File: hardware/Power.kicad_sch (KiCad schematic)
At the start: 51 parts, among them U10 LDK320ADU120R, U4 TPS563300DRLR, U5 TPS563219ADDFR, U6 LM2940SX-12_NOPB, U7 LM1117IMP-5.0, U8 TLV743P, U9 AP2127N3-1.5

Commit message: Added Voltage reference, fixed silkscreen and BOM
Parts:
- U5: footprint SOT65P280X110-8N -> TPS563219ADDFR:SOT65P280X110-8N
- U6: footprint KTT0003B -> DDPAK:KTT0003B
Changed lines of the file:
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@@
 			)
 		)
-		(property "Datasheet" "~"
+		(property "Datasheet" "---"
 			(at 77.47 166.37 0)
 			(effects
@@
 			)
 		)
-		(property "Datasheet" "~"
+		(property "Datasheet" "---"
 			(at 208.28 119.38 0)
 			(effects
@@
 			)
 		)
-		(property "Footprint" "KTT0003B"
+		(property "Footprint" "DDPAK:KTT0003B"
 			(at 66.04 214.3 0)
 			(effects
@@
 			)
 		)
-		(property "Datasheet" "~"
+		(property "Datasheet" "---"
 			(at 163.83 35.56 0)
 			(effects
@@
 			)
 		)
-		(property "Datasheet" "~"
+		(property "Datasheet" "---"
 			(at 139.7 119.38 0)
 			(effects
@@
 			)
 		)
-		(property "Datasheet" "~"
+		(property "Datasheet" "---"
 			(at 144.78 166.37 0)
 			(effects
@@
 			)
 		)
-		(property "Datasheet" "~"
+		(property "Datasheet" "---"
 			(at 152.4 73.66 0)
 			(effects
@@
 			)
 		)
-		(property "Datasheet" "https://www.littelfuse.com/assetdocs/littelfuse_fuse_466_datasheet?assetguid=dbe9bcd7-6072-4adf-bf5b-d33e52a6b90f"
+		(property "Datasheet" "https://www.mouser.pl/datasheet/3/40/1/sf0603f.pdf"
 			(at 95.25 119.38 0)
 			(effects
@@
 			)
 		)
-		(property "Footprint" "SOT65P280X110-8N"
+		(property "Footprint" "TPS563219ADDFR:SOT65P280X110-8N"
 			(at 95.25 168.58 0)
 			(effects
@@
 			)
 		)
-		(property "Datasheet" "~"
+		(property "Datasheet" "---"
 			(at 68.58 119.38 0)
 			(effects

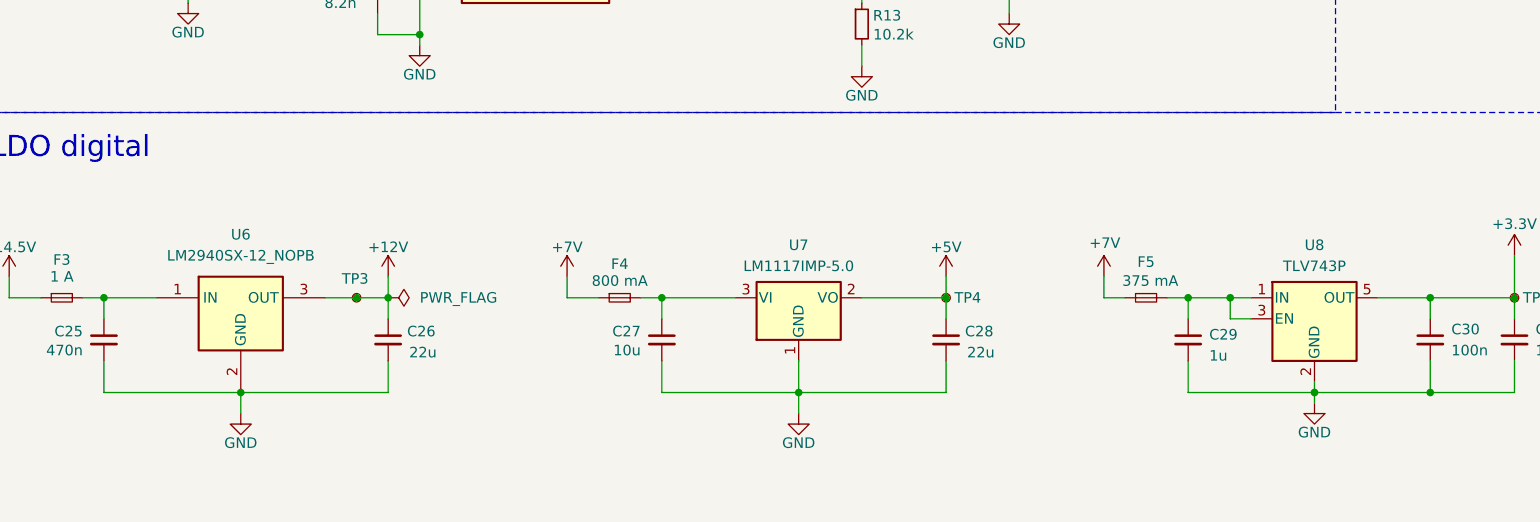
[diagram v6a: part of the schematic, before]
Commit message: Changed some components - they were non stocked
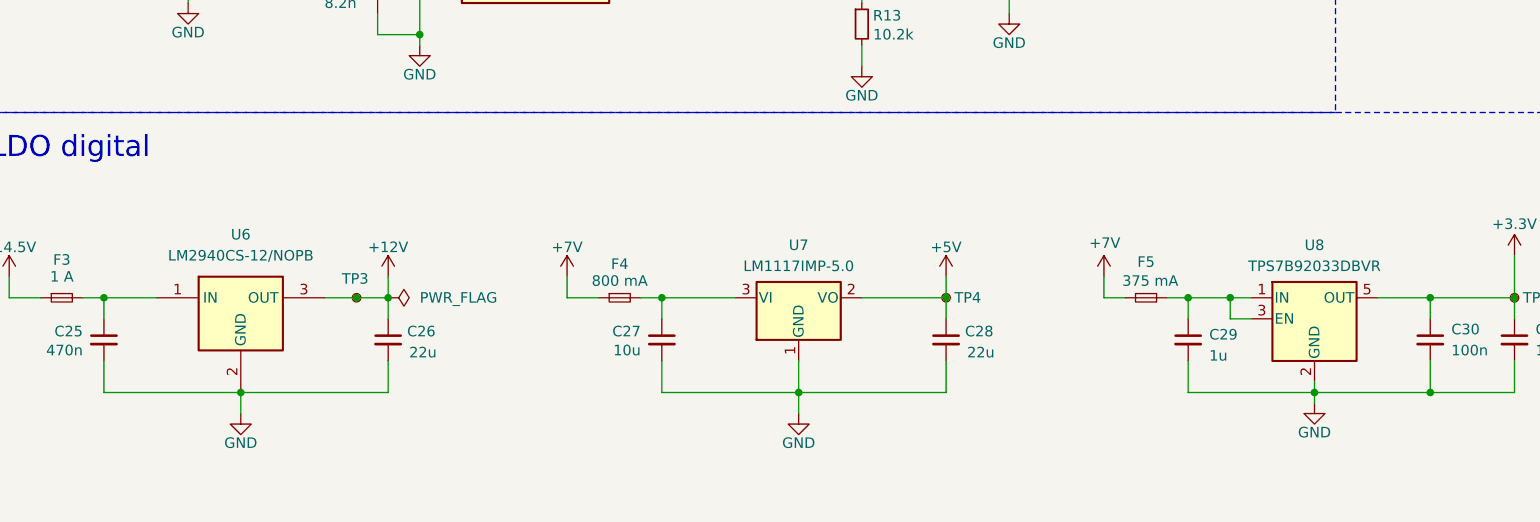
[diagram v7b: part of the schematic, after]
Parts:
- C21: Manufacturer_Part_Number C0402C103K1RACAUTO7411 -> GA0603Y822KXBAC31G; Mouser https://www.mouser.pl/ProductDetail/KEMET/C0402C103K1RACAUT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 -> https://www.mouser.pl/ProductDetail/Vishay-Vitramon/GA0603Y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; Mouser No 80-C0402C103K1RAUTO7 -> 77-GA603Y822KXBAC31G
- C25: Manufacturer_Part_Number GRT188R61H105KE13D -> GRM188R61H474KA12D; Mouser https://www.mouser.pl/ProductDetail/Murata-Electronics/GRT1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 -> https://www.mouser.pl/ProductDetail/Murata-Electronics/GRM1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; Mouser No 81-GRT188R61H105KE3D -> 81-GRM188R61H474KA2D
- C32, C34, C35, C36: Manufacturer_Part_Number TMCP1A475KTRF -> GRM188R61H225KE11D; Mouser https://www.mouser.pl/ProductDetail/Vishay-Sprague/TMCP1A47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 -> https://www.mouser.pl/ProductDetail/Murata-Electronics/GRM1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; Mouser No 74-TMCP1A475KTRF -> 81-GRM188R61H225KE1D
- U6: value LM2940SX-12_NOPB -> LM2940CS-12/NOPB; Manufacturer_Part_Number LM2940SX-12/NOPB -> LM2940CS-12/NOPB; Mouser https://www.mouser.pl/ProductDetail/Texas-Instruments/LM2940SX-12-NOPB?qs=X1J7HmVL2ZEie6RRCswWNw%3D%3D -> https://www.mouser.pl/ProductDetail/Texas-Instruments/LM2940CS-12-NOPB?qs=X1J7HmVL2ZHJ746w5J93Ow%3D%3D; Mouser No 926-LM2940SX-12/NOPB -> 926-LM2940CS-12/NOPB
- U8: value TLV743P -> TPS7B92033DBVR; Manufacturer_Part_Number TLV74333PDBVR -> TPS7B92033DBVR; Mouser https://www.mouser.pl/ProductDetail/Texas-Instruments/TLV74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 -> https://www.mouser.pl/ProductDetail/Texas-Instruments/TPS7B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; Mouser No 595-TLV74333PDBVR -> 595-TPS7B92033DBVR
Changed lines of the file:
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@@
 			)
 		)
-		(property "Datasheet" "https://www.vishay.com/docs/40179/tmcp.pdf"
+		(property "Datasheet" "https://pim.murata.com/asset/pim4/ceramicCapacitorSMD/GRM188R61H225KE11-01A-EN_PDF_CERAMICCAPACITORSMD"
 			(at 139.7 171.45 0)
 			(effects
@@
 			)
 		)
-		(property "Mouser" "https://www.mouser.pl/ProductDetail/Vishay-Sprague/TMCP1A475KTRF?qs=WatphXlIDnx98Nc1%252Bo65LQ%3D%3D"
+		(property "Mouser" "https://www.mouser.pl/ProductDetail/Murata-Electronics/GRM188R61H225KE11D?qs=eeBpzGFlv%252B%2Fz%2FOAJ2DfLOw%3D%3D"
 			(at 139.7 171.45 0)
 			(effects
@@
 			)
 		)
-		(property "Mouser No" "74-TMCP1A475KTRF"
+		(property "Mouser No" "81-GRM188R61H225KE1D"
 			(at 139.7 171.45 0)
 			(effects
@@
 			)
 		)
-		(property "Manufacturer_Part_Number" "TMCP1A475KTRF"
+		(property "Manufacturer_Part_Number" "GRM188R61H225KE11D"
 			(at 139.7 171.45 0)
 			(effects
@@
 			)
 		)
-		(property "Datasheet" "https://www.vishay.com/docs/40179/tmcp.pdf"
+		(property "Datasheet" "https://pim.murata.com/asset/pim4/ceramicCapacitorSMD/GRM188R61H225KE11-01A-EN_PDF_CERAMICCAPACITORSMD"
 			(at 72.39 171.45 0)
 			(effects
@@
 			)
 		)
-		(property "Mouser" "https://www.mouser.pl/ProductDetail/Vishay-Sprague/TMCP1A475KTRF?qs=WatphXlIDnx98Nc1%252Bo65LQ%3D%3D"
+		(property "Mouser" "https://www.mouser.pl/ProductDetail/Murata-Electronics/GRM188R61H225KE11D?qs=eeBpzGFlv%252B%2Fz%2FOAJ2DfLOw%3D%3D"
 			(at 72.39 171.45 0)
 			(effects
@@
 			)
 		)
-		(property "Mouser No" "74-TMCP1A475KTRF"
+		(property "Mouser No" "81-GRM188R61H225KE1D"
 			(at 72.39 171.45 0)
 			(effects
@@
 			)
 		)
-		(property "Manufacturer_Part_Number" "TMCP1A475KTRF"
+		(property "Manufacturer_Part_Number" "GRM188R61H225KE11D"
 			(at 72.39 171.45 0)
 			(effects
@@
 			)
 		)
-		(property "Value" "LM2940SX-12_NOPB"
+		(property "Value" "LM2940CS-12/NOPB"
 			(at 49.53 114.3 0)
 			(effects
@@
 			)
 		)
-		(property "Datasheet" "http://www.ti.com/lit/gpn/lm2940-n"
+		(property "Datasheet" "https://www.ti.com/lit/ds/symlink/lm2940c.pdf?ts=1773909097676&ref_url=https%253A%252F%252Fro.mouser.com%252F"
 			(at 66.04 314.3 0)
 			(effects
@@
 			)
 		)
-		(property "Manufacturer_Part_Number" "LM2940SX-12/NOPB"
+		(property "Manufacturer_Part_Number" "LM2940CS-12/NOPB"
 			(at 66.04 914.3 0)
 			(effects
@@
 			)
 		)
-		(property "Mouser" "https://www.mouser.pl/ProductDetail/Texas-Instruments/LM2940SX-12-NOPB?qs=X1J7HmVL2ZEie6RRCswWNw%3D%3D"
+		(property "Mouser" "https://www.mouser.pl/ProductDetail/Texas-Instruments/LM2940CS-12-NOPB?qs=X1J7HmVL2ZHJ746w5J93Ow%3D%3D"
 			(at 39.37 119.38 0)
 			(effects
@@
 			)
 		)
-		(property "Mouser No" "926-LM2940SX-12/NOPB"
+		(property "Mouser No" "926-LM2940CS-12/NOPB"
 			(at 39.37 119.38 0)
 			(effects
@@
 			)
 		)
-		(property "Datasheet" "https://pim.murata.com/asset/pim4/ceramicCapacitorSMD/GRT188R61H105KE13-01A-EN_PDF_CERAMICCAPACITORSMD"
+		(property "Datasheet" "https://pim.murata.com/asset/pim4/ceramicCapacitorSMD/GRM188R61H474KA12-04A-EN_PDF_CERAMICCAPACITORSMD"
 			(at 33.02 124.46 0)
 			(effects
@@
 			)
 		)
-		(property "Mouser" "https://www.mouser.pl/ProductDetail/Murata-Electronics/GRT188R61H105KE13D?qs=drgMNd%252BkGPNIxxtJByMGCg%3D%3D"
+		(property "Mouser" "https://www.mouser.pl/ProductDetail/Murata-Electronics/GRM188R61H474KA12D?qs=4W3PNmGdEWHPXU2UiOr6Bg%3D%3D"
 			(at 33.02 124.46 0)
 			(effects
@@
 			)
 		)
-		(property "Mouser No" "81-GRT188R61H105KE3D"
+		(property "Mouser No" "81-GRM188R61H474KA2D"
 			(at 33.02 124.46 0)
 			(effects
@@
 			)
 		)
-		(property "Manufacturer_Part_Number" "GRT188R61H105KE13D"
+		(property "Manufacturer_Part_Number" "GRM188R61H474KA12D"
 			(at 33.02 124.46 0)
 			(effects
@@
 			)
 		)
-		(property "Datasheet" "https://www.vishay.com/docs/40179/tmcp.pdf"
+		(property "Datasheet" "https://pim.murata.com/asset/pim4/ceramicCapacitorSMD/GRM188R61H225KE11-01A-EN_PDF_CERAMICCAPACITORSMD"
 			(at 105.41 171.45 0)
 			(effects
@@
 			)
 		)
-		(property "Mouser" "https://www.mouser.pl/ProductDetail/Vishay-Sprague/TMCP1A475KTRF?qs=WatphXlIDnx98Nc1%252Bo65LQ%3D%3D"
+		(property "Mouser" "https://www.mouser.pl/ProductDetail/Murata-Electronics/GRM188R61H225KE11D?qs=eeBpzGFlv%252B%2Fz%2FOAJ2DfLOw%3D%3D"
 			(at 105.41 171.45 0)
 			(effects
@@
 			)
 		)
-		(property "Mouser No" "74-TMCP1A475KTRF"
+		(property "Mouser No" "81-GRM188R61H225KE1D"
 			(at 105.41 171.45 0)
 			(effects
@@
 			)
 		)
-		(property "Manufacturer_Part_Number" "TMCP1A475KTRF"
+		(property "Manufacturer_Part_Number" "GRM188R61H225KE11D"
 			(at 105.41 171.45 0)
 			(effects
@@
 			)
 		)
-		(property "Datasheet" "https://www.vishay.com/docs/40179/tmcp.pdf"
+		(property "Datasheet" "https://pim.murata.com/asset/pim4/ceramicCapacitorSMD/GRM188R61H225KE11-01A-EN_PDF_CERAMICCAPACITORSMD"
 			(at 38.1 171.45 0)
 			(effects
@@
 			)
 		)
-		(property "Mouser" "https://www.mouser.pl/ProductDetail/Vishay-Sprague/TMCP1A475KTRF?qs=WatphXlIDnx98Nc1%252Bo65LQ%3D%3D"
+		(property "Mouser" "https://www.mouser.pl/ProductDetail/Murata-Electronics/GRM188R61H225KE11D?qs=eeBpzGFlv%252B%2Fz%2FOAJ2DfLOw%3D%3D"
 			(at 38.1 171.45 0)
 			(effects
@@
 			)
 		)
-		(property "Mouser No" "74-TMCP1A475KTRF"
+		(property "Mouser No" "81-GRM188R61H225KE1D"
 			(at 38.1 171.45 0)
 			(effects
@@
 			)
 		)
-		(property "Manufacturer_Part_Number" "TMCP1A475KTRF"
+		(property "Manufacturer_Part_Number" "GRM188R61H225KE11D"
 			(at 38.1 171.45 0)
 			(effects
@@
 			)
 		)
-		(property "Datasheet" "https://www.mouser.pl/datasheet/3/508/1/KEM_C1023_X7R_AUTO_SMD.pdf"
+		(property "Datasheet" "https://www.vishay.com/docs/45230/ga31gautomlccsold.pdf"
 			(at 66.04 82.55 0)
 			(effects
@@
 			)
 		)
-		(property "Mouser" "https://www.mouser.pl/ProductDetail/KEMET/C0402C103K1RACAUTO7411?qs=ulEaXIWI0c8Eh%252BkW3Sqcaw%3D%3D"
+		(property "Mouser" "https://www.mouser.pl/ProductDetail/Vishay-Vitramon/GA0603Y822KXBAC31G?qs=uwxL4vQweFMqjEqq6rLJiA%3D%3D"
 			(at 66.04 82.55 0)
 			(effects
@@
 			)
 		)
-		(property "Mouser No" "80-C0402C103K1RAUTO7"
+		(property "Mouser No" "77-GA603Y822KXBAC31G"
 			(at 66.04 82.55 0)
 			(effects
@@
 			)
 		)
-		(property "Manufacturer_Part_Number" "C0402C103K1RACAUTO7411"
+		(property "Manufacturer_Part_Number" "GA0603Y822KXBAC31G"
 			(at 66.04 82.55 0)
 			(effects
@@
 			)
 		)
-		(property "Value" "TLV743P"
+		(property "Value" "TPS7B92033DBVR"
 			(at 179.07 115.57 0)
 			(effects
@@
 			)
 		)
-		(property "Datasheet" "https://www.ti.com/lit/ds/symlink/tlv743p.pdf"
+		(property "Datasheet" "https://www.ti.com/lit/ds/symlink/tps7b92.pdf"
 			(at 179.07 121.92 0)
 			(effects
@@
 			)
 		)
-		(property "Mouser" "https://www.mouser.pl/ProductDetail/Texas-Instruments/TLV74333PDBVR?qs=EU6FO9ffTwe08kePOwcQGA%3D%3D"
+		(property "Mouser" "https://www.mouser.pl/ProductDetail/Texas-Instruments/TPS7B92033DBVR?qs=i8QVZAFTkqTn75tUVrN19A%3D%3D"
 			(at 179.07 121.92 0)
 			(effects
@@
 			)
 		)
-		(property "Manufacturer_Part_Number" "TLV74333PDBVR"
+		(property "Manufacturer_Part_Number" "TPS7B92033DBVR"
 			(at 179.07 121.92 0)
 			(effects
@@
 			)
 		)
-		(property "Mouser No" "595-TLV74333PDBVR"
+		(property "Mouser No" "595-TPS7B92033DBVR"
 			(at 179.07 121.92 0)
 			(effects

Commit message: Footprints files cleanup
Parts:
- U10: footprint Package_TO_SOT_SMD:SOT-89-3_Handsoldering -> LDO_12V:SOT-89-3_Handsoldering
- U9: footprint Package_TO_SOT_SMD:TSOT-23_HandSoldering -> LDO_5V:TSOT-23_HandSoldering
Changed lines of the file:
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@@
 			)
 		)
-		(property "Footprint" "Package_TO_SOT_SMD:SOT-89-3_Handsoldering"
+		(property "Footprint" "LDO_12V:SOT-89-3_Handsoldering"
 			(at 121.92 161.29 0)
 			(effects
@@
 			)
 		)
-		(property "Footprint" "Package_TO_SOT_SMD:TSOT-23_HandSoldering"
+		(property "Footprint" "LDO_5V:TSOT-23_HandSoldering"
 			(at 54.61 160.655 0)
 			(effects
